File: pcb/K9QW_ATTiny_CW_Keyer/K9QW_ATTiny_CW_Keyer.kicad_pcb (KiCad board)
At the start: 2 copper layers, 57.2 x 50.8 mm, 30 parts, among them J1 Paddle Input, J10 Mounting Hole, J2 Key Output, J4 Sidetone, J5 Barrel_Jack_MountingPin, J9 Power Input, Q1 MMBT2222A, Q2 MMBT3904, Q3 MMBT3904, SW1 Command, SW2 Power Switch, U1 ATtiny85-20P, U2 LD1117S33TR_SOT223

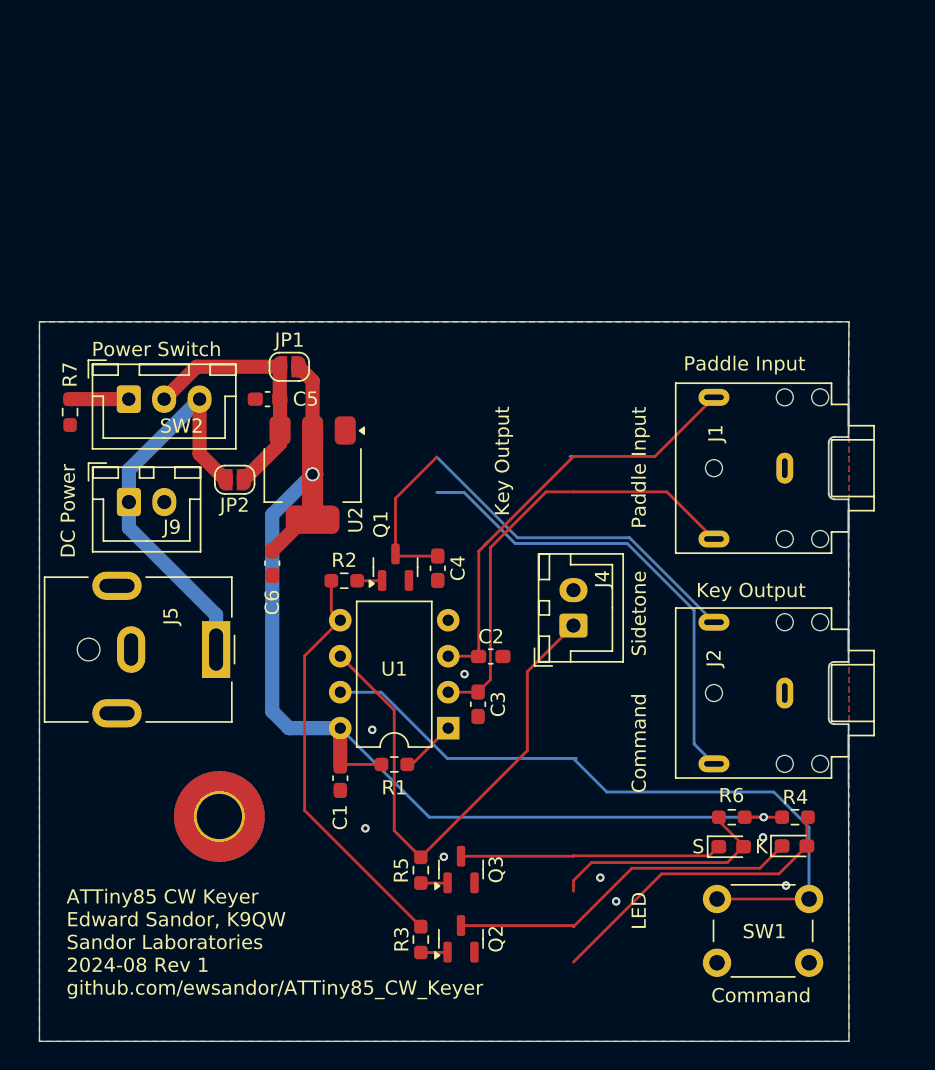
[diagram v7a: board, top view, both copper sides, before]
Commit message: Removed panel headers, added reverse polarity protection, rough layout
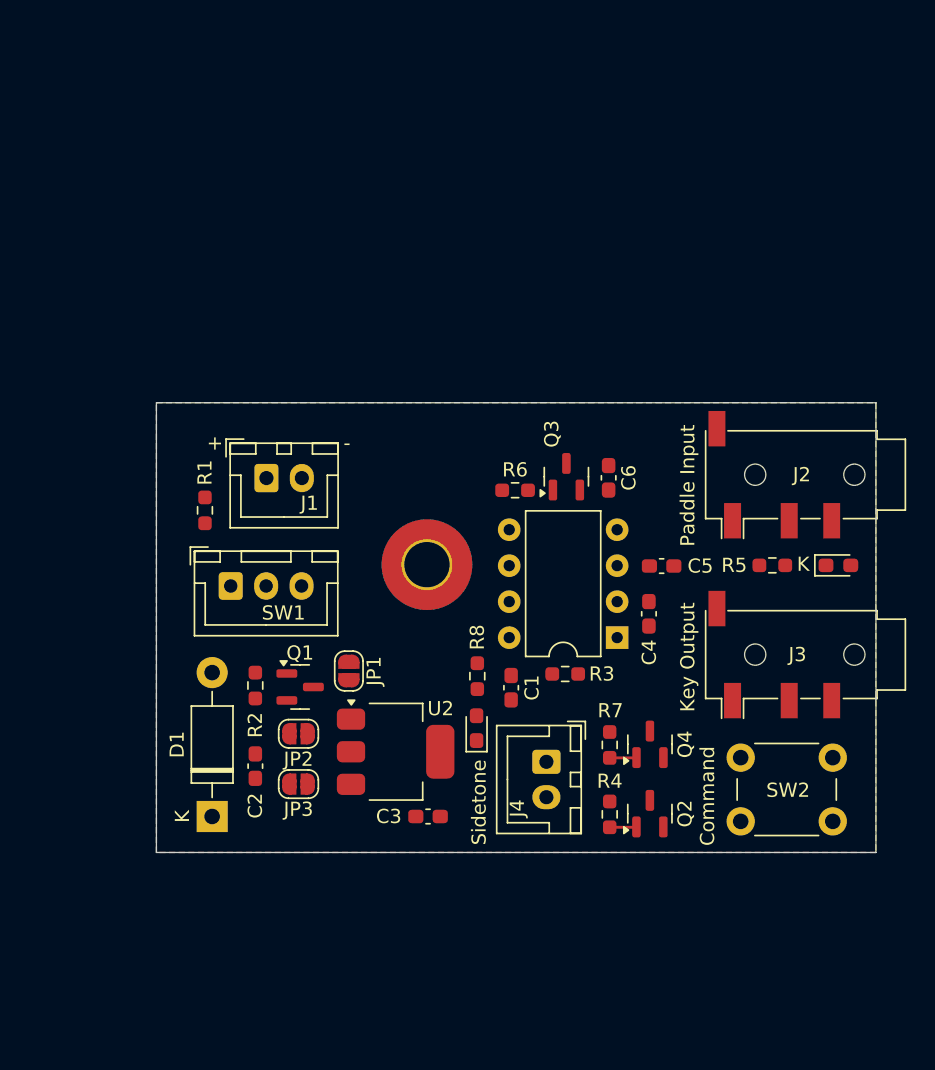
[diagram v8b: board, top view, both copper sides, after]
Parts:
- removed the J1 at (170.9, 90.7)
- removed the J5 at (130.7, 103.5)
- added D1: 1N4741A, Diode_THT:D_DO-41_SOD81_P10.16mm_Horizontal, F.Cu at (130.4, 115.3)
- added J3: AudioJack4, Connector_Audio:Jack_3.5mm_PJ320D_Horizontal, F.Cu at (171.0, 103.9)
- added JP2: Bypass Polarity Protection, Jumper:SolderJumper-2_P1.3mm_Open_RoundedPad1.0x1.5mm, F.Cu at (136.5, 109.5)
- added Q1: AO3401A, Package_TO_SOT_SMD:SOT-23, F.Cu at (136.6, 106.2)
- added R2: 10k, Resistor_SMD:R_0603_1608Metric_Pad0.98x0.95mm_HandSolder, F.Cu at (133.5, 106.1)
- J2: value Key Output -> AudioJack4; footprint Connector_Audio:Jack_3.5mm_CUI_SJ1-3523N_Horizontal -> Connector_Audio:Jack_3.5mm_PJ320D_Horizontal
- moved JP3 29.5 mm to (136.5, 113.0)
- moved C2 25.9 mm to (133.5, 111.8), turned to -90 degrees
- moved J5 23.0 mm to (145.6, 97.5)
- moved C3 21.0 mm to (145.7, 115.3), turned to 180 degrees
- moved R8 20.5 mm to (149.1, 105.4), turned to 90 degrees
- moved U2 20.4 mm to (143.4, 110.7), turned to 0 degrees
- moved D2 20.1 mm to (174.6, 97.6)
- moved D3 19.8 mm to (149.1, 109.1), turned to 90 degrees
- moved R5 17.9 mm to (170.0, 97.6)
- moved Q4 16.0 mm to (161.3, 110.2)
- moved R4 16.0 mm to (158.5, 115.2)
- moved R7 16.0 mm to (158.5, 110.3)
- moved Q2 16.0 mm to (161.3, 115.1)
- moved JP1 15.7 mm to (140.1, 105.0), turned to 90 degrees
- moved J2 15.4 mm to (171.0, 91.2), turned to 180 degrees
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- renumbered C5 to C2, C6 to C3, C3 to C4, C2 to C5, C4 to C6, D1 to D2, D2 to D3, J9 to J1, J10 to J5, JP2 to JP1, JP1 to JP3, Q1 to Q3, Q3 to Q4, R7 to R1, R1 to R3, R3 to R4, R4 to R5, R2 to R6, R5 to R7, R6 to R8, SW2 to SW1, SW1 to SW2
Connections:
- C2 pad 1: Net-(JP1-A) -> Net-(D1-K)
- C6 pad 1: KEY Out -> Net-(Q3-C)
- J2 pad T: KEY Out -> DIT
- JP3 pad 1: Net-(JP1-A) -> Net-(D1-K)
- Q3 pad 3: KEY Out -> Net-(Q3-C)
- U2 pad 3: Net-(JP1-A) -> Net-(D1-K)
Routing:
- net VCC: track 79.7 -> 0.15 mm, vias 2 -> 0
- net COMMAND: track 48.8 -> 0.00 mm
- net SIDETONE: track 37.4 -> 0.00 mm
- net KEY Out: track 35.5 -> 0.00 mm
- net KEY Ring: track 33.0 -> 0.00 mm
- net DAH: track 31.5 -> 0.00 mm
- net DIT: track 31.2 -> 0.00 mm
- net KEY: track 29.1 -> 0.00 mm
- net VDC: track 28.7 -> 0.00 mm
- net Net-(D2-K): track 25.1 -> 0.00 mm
- net Net-(D2-A): track 21.9 -> 0.00 mm
- net Net-(D3-K): track 18.5 -> 0.00 mm
- net Net-(JP1-A): track 18.2 -> 0.00 mm
- net Net-(D3-A): track 16.6 -> 0.00 mm
- net Net-(SW1-A): track 4.14 -> 0.00 mm
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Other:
- board size 57.2 x 50.8 mm -> 50.8 x 31.8 mm
- board text added: "+"
- board text added: "-"
- board text added: "ATTiny85 CW Keyer PCB by Edward Sandor, K9QW Sandor Laboratories 2024-08 Rev 1 github.com/ewsandor/ATTiny85_CW_Keyer"
- board text removed: "ATTiny85 CW Keyer Edward Sandor, K9QW Sandor Laboratories 2024-08 Rev 1 github.com/ewsandor/ATTiny85_CW_Keyer"
- board text removed: "DC Power"
- board text removed: "LED"
- board text removed: "Power Switch"
- board text removed: "S"
